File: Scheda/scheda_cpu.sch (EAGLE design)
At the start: 21 parts, among them IC3 LD1117V33

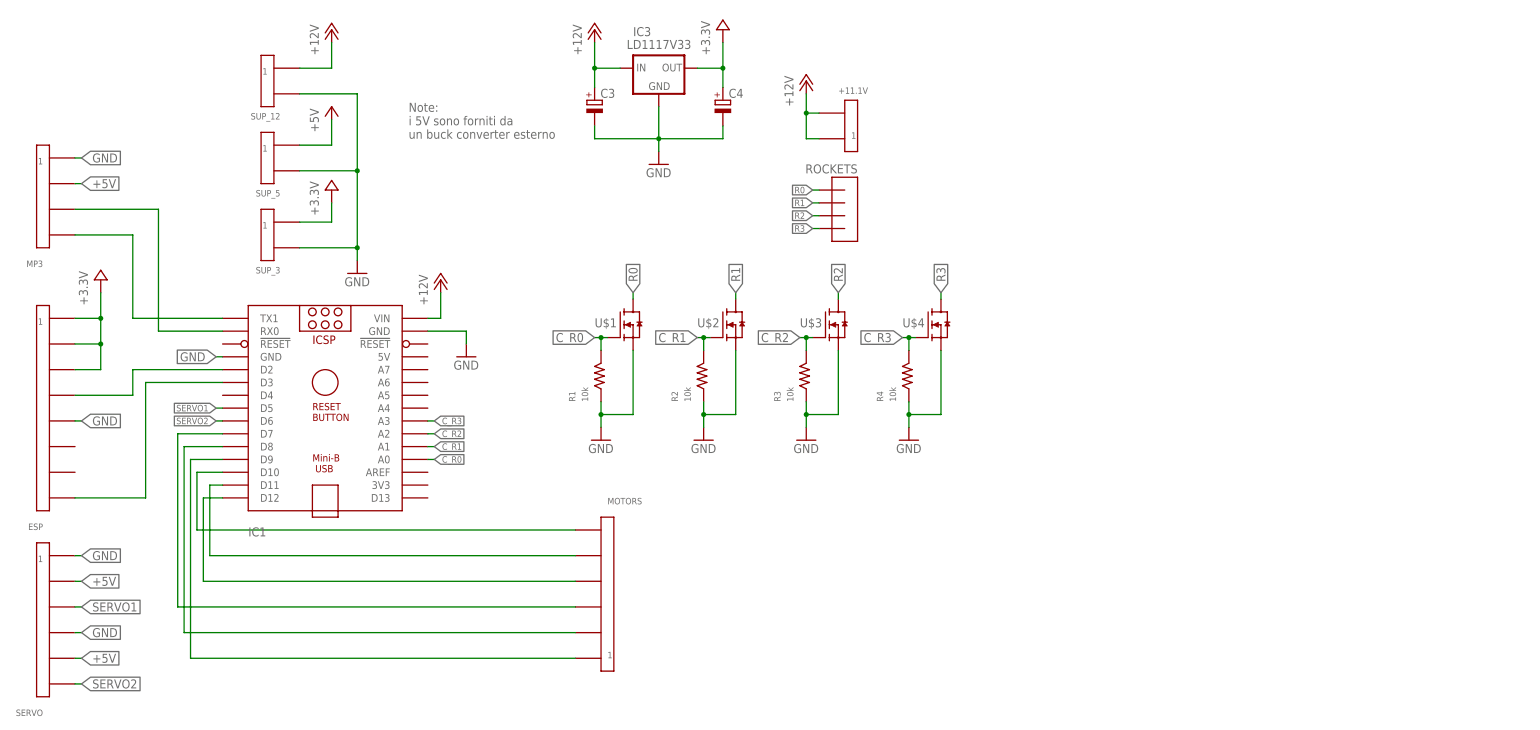
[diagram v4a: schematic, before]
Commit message: completato pcb con lm380
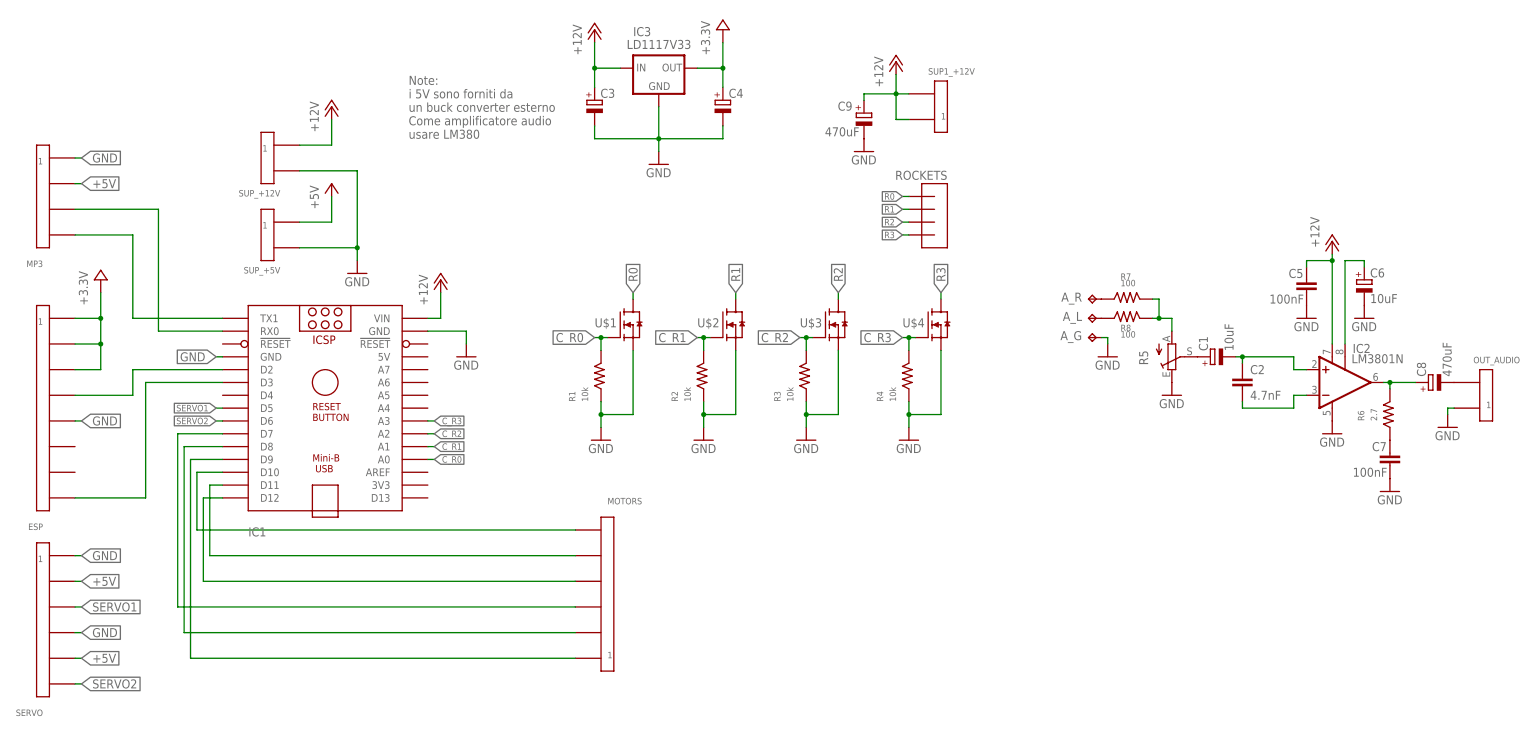
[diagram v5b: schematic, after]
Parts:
- removed +11.1V, SUP_12: AK500, roombarmato_eagle_lib:AK500
- added A_G, A_L, A_R: TPTP15SQ, testpad:TPTP15SQ
- added C1, C6: 10uF, roombarmato_eagle_lib:CPOL-EUE2.5-5
- added C2: 4.7nF, ITIS:C-EU025-030X050
- added C5, C7: 100nF, ITIS:C-EU025-030X050
- added C8, C9: 470uF, roombarmato_eagle_lib:CPOL-EUE2.5-5
- added IC2: LM3801N, roombarmato_eagle_lib:LM3801N
- added OUT_AUDIO, SUP1_+12V: AK500, roombarmato_eagle_lib:AK500
- added R5: (no value), pot:TRIM_EU-S64W
- added R6: 2.7, roombarmato_eagle_lib:RESISTOR1206
- added R7, R8: 100, roombarmato_eagle_lib:RESISTOR1206
- renumbered SUP_3 to SUP_+5V, SUP_5 to SUP_+12V
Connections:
- new net IN_AUDIO: R5.A, R7.P$2, R8.P$2
- new net N$10: C8.+, IC2.OUT, R6.P$2
- new net N$17: C8.-, OUT_AUDIO.P$2
- new net N$18: A_R.TP, R7.P$1
- new net N$19: A_L.TP, R8.P$1
- new net N$5: C1.+, R5.S
- new net N$6: C1.-, C2.1, IC2.+IN
- new net N$7: C2.2, IC2.-IN
- new net N$8: C6.+, IC2.BYPASS
- new net N$9: C7.1, R6.P$1
- net +12V: now also C5.1, C9.+, IC2.VSS, SUP1_+12V.P$1, SUP1_+12V.P$2, SUP_+12V.P$1; no longer +11.1V.P$1, +11.1V.P$2, SUP_12.P$1
- net +3.3V: no longer SUP_+5V.P$1
- net +5V: now also SUP_+5V.P$1; no longer SUP_+12V.P$1
- net GND: now also A_G.TP, C5.2, C6.-, C7.2, C9.-, IC2.GND, OUT_AUDIO.P$1, R5.E; no longer SUP_12.P$2
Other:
- note added: "Note: i 5V sono forniti da un buck converter esterno Come amplificatore audio usare LM380"
- note removed: "Note: i 5V sono forniti da un buck converter esterno"
- moved on the sheet: ROCKETS

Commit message: creato file excel ordine
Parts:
- C1, C6: device roombarmato_eagle_lib:CPOL-EUE2.5-5 -> ITIS:CPOL-EUE2-4
- C8: device roombarmato_eagle_lib:CPOL-EUE2.5-5 -> ITIS:CPOL-EUE3.5-8
- C9: value 470uF -> 1000uF; device roombarmato_eagle_lib:CPOL-EUE2.5-5 -> ITIS:CPOL-EUE3.5-10
- R5: value (none) -> 10k
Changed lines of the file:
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@@
 <part name="P+6" library="roombarmato_eagle_lib" deviceset="+12V" device=""/>
 <part name="IC2" library="roombarmato_eagle_lib" deviceset="LM380" device="N" package3d_urn="urn:adsk.eagle:package:16409/2" technology="1"/>
-<part name="R5" library="pot" library_urn="urn:adsk.eagle:library:331" deviceset="TRIM_EU-" device="S64W" package3d_urn="urn:adsk.eagle:package:22708/1"/>
+<part name="R5" library="pot" library_urn="urn:adsk.eagle:library:331" deviceset="TRIM_EU-" device="S64W" package3d_urn="urn:adsk.eagle:package:22708/1" value="10k"/>
 <part name="GND7" library="roombarmato_eagle_lib" deviceset="GND" device=""/>
-<part name="C1" library="roombarmato_eagle_lib" deviceset="CPOL-EU" device="E2.5-5" value="10uF"/>
+<part name="C1" library="ITIS" deviceset="CPOL-EU" device="E2-4" value="10uF"/>
 <part name="C2" library="ITIS" deviceset="C-EU" device="025-030X050" value="4.7nF"/>
 <part name="GND9" library="roombarmato_eagle_lib" deviceset="GND" device=""/>
 <part name="P+3" library="roombarmato_eagle_lib" deviceset="+12V" device=""/>
 <part name="GND10" library="roombarmato_eagle_lib" deviceset="GND" device=""/>
-<part name="C6" library="roombarmato_eagle_lib" deviceset="CPOL-EU" device="E2.5-5" value="10uF"/>
+<part name="C6" library="ITIS" deviceset="CPOL-EU" device="E2-4" value="10uF"/>
 <part name="GND11" library="roombarmato_eagle_lib" deviceset="GND" device=""/>
 <part name="R6" library="roombarmato_eagle_lib" deviceset="RESISTOR" device="1206" package3d_urn="urn:adsk.eagle:package:17825322/7" value="2.7"/>
@@
 <part name="C7" library="ITIS" deviceset="C-EU" device="025-030X050" value="100nF"/>
 <part name="GND12" library="roombarmato_eagle_lib" deviceset="GND" device=""/>
-<part name="C8" library="roombarmato_eagle_lib" deviceset="CPOL-EU" device="E2.5-5" value="470uF"/>
+<part name="C8" library="ITIS" deviceset="CPOL-EU" device="E3.5-8" value="470uF"/>
 <part name="OUT_AUDIO" library="roombarmato_eagle_lib" deviceset="AK500" device="" package3d_urn="urn:adsk.eagle:package:17855270/2"/>
 <part name="GND13" library="roombarmato_eagle_lib" deviceset="GND" device=""/>
@@
 <part name="A_G" library="testpad" library_urn="urn:adsk.eagle:library:385" deviceset="TP" device="TP15SQ" package3d_urn="urn:adsk.eagle:package:27975/1" value="TPTP15SQ"/>
 <part name="GND14" library="roombarmato_eagle_lib" deviceset="GND" device=""/>
-<part name="C9" library="roombarmato_eagle_lib" deviceset="CPOL-EU" device="E2.5-5" value="470uF"/>
+<part name="C9" library="ITIS" deviceset="CPOL-EU" device="E3.5-10" value="1000uF"/>
 <part name="GND15" library="roombarmato_eagle_lib" deviceset="GND" device=""/>
 </parts>
@@
 </instance>
 <instance part="R5" gate="1" x="167.64" y="5.08" smashed="yes" rot="MR180">
-<attribute name="NAME" x="162.941" y="6.35" size="1.778" layer="95" rot="MR270"/>
-<attribute name="VALUE" x="163.83" y="8.89" size="1.778" layer="96" rot="MR270"/>
+<attribute name="NAME" x="161.671" y="6.35" size="1.778" layer="95" rot="MR270"/>
+<attribute name="VALUE" x="163.83" y="6.35" size="1.778" layer="96" rot="MR270"/>
 </instance>
 <instance part="GND7" gate="1" x="167.64" y="-2.54" smashed="yes">
@@
 <instance part="C9" gate="G$1" x="106.68" y="53.34" smashed="yes">
 <attribute name="NAME" x="101.473" y="53.8226" size="1.778" layer="95"/>
-<attribute name="VALUE" x="98.933" y="48.7426" size="1.778" layer="96"/>
+<attribute name="VALUE" x="97.663" y="48.7426" size="1.778" layer="96"/>
 </instance>
 <instance part="GND15" gate="1" x="106.68" y="45.72" smashed="yes">

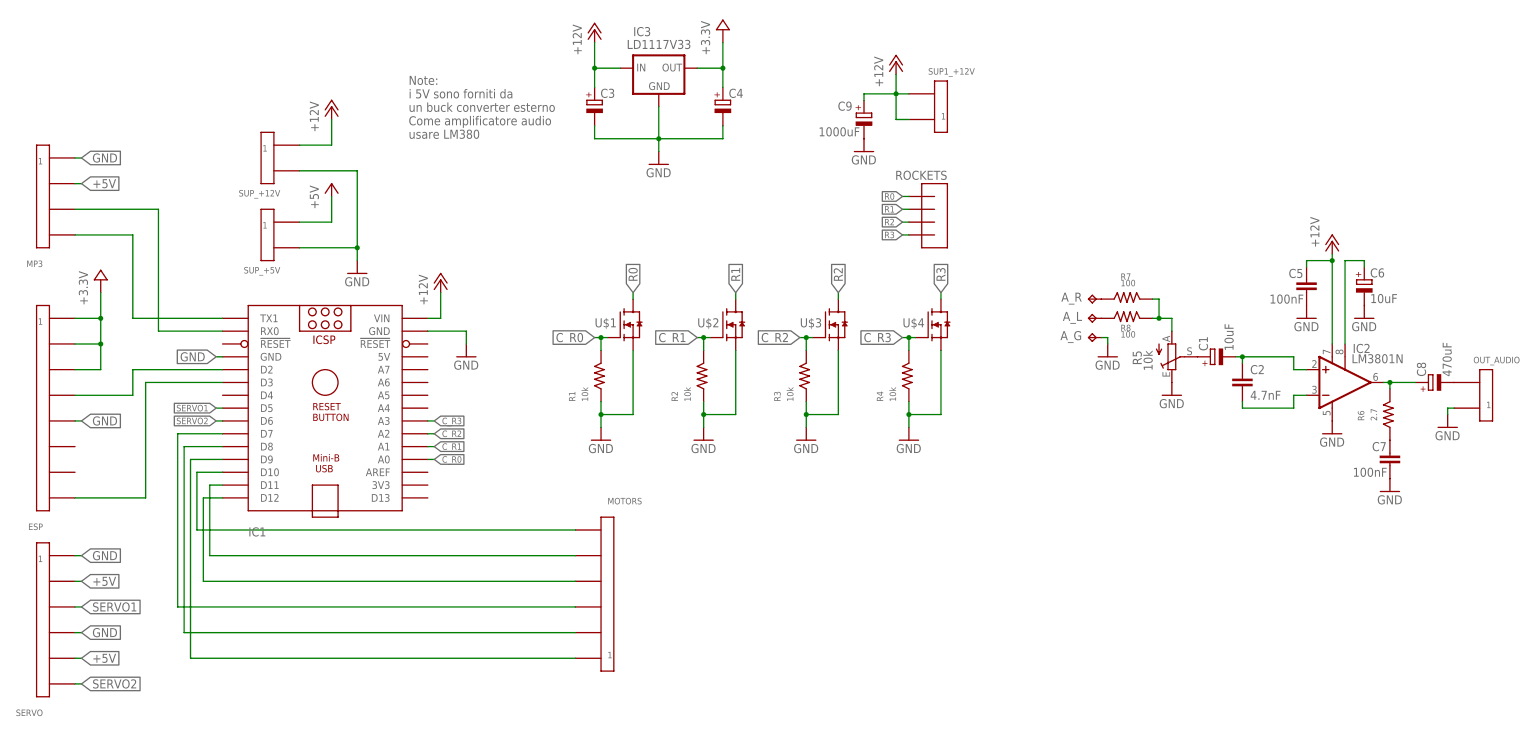
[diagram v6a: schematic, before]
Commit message: aggiunte etichette su pcb
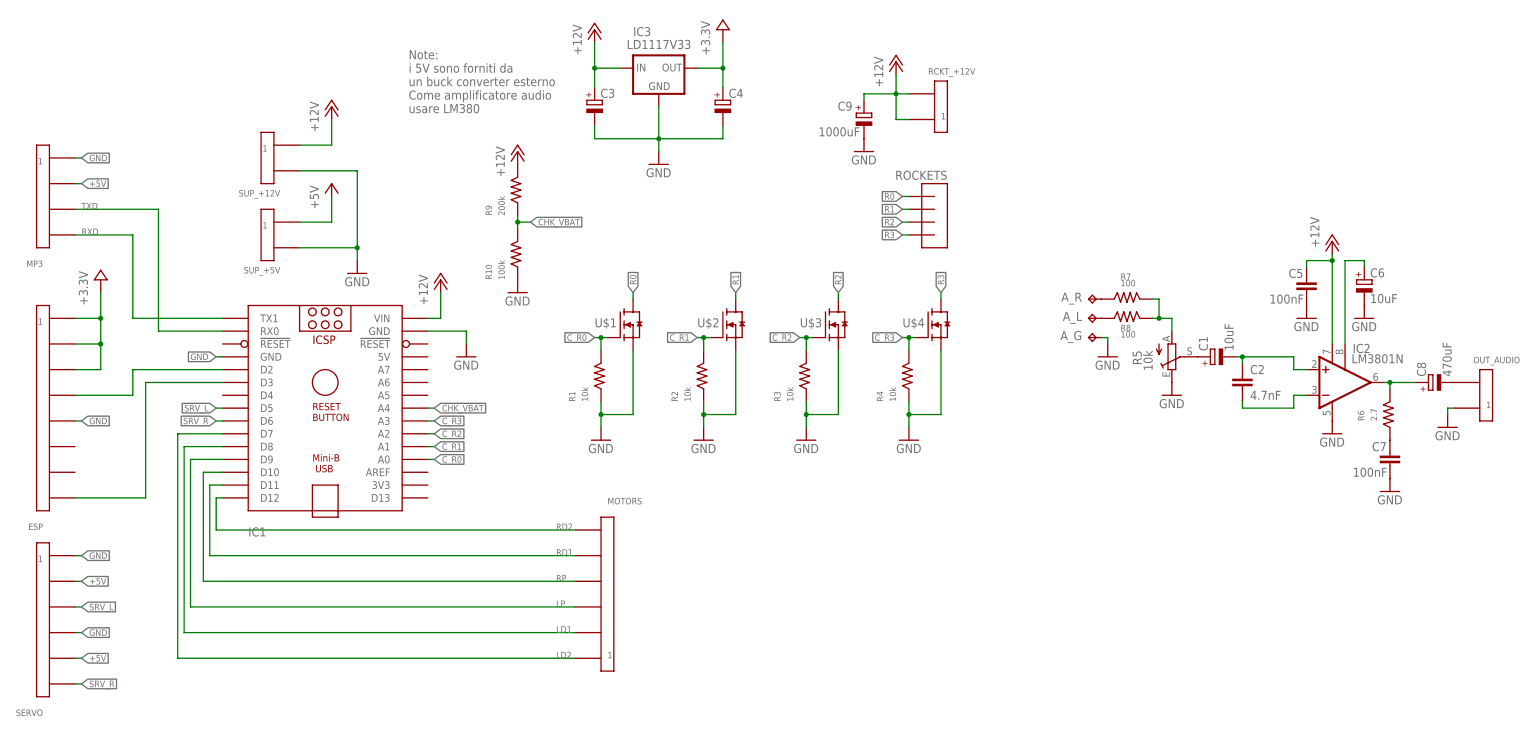
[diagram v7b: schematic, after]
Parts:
- added R10: 100k, roombarmato_eagle_lib:RESISTOR1206
- added R9: 200k, roombarmato_eagle_lib:RESISTOR1206
- renumbered SUP1_+12V to RCKT_+12V
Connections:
- net N$13 renamed LD1
- net N$16 renamed RD1
- net N$2 renamed TXD
- net N$3 renamed RXD
- net SERVO1 renamed SRV_L
- net SERVO2 renamed SRV_R
- removed net N$11: IC1.D10, MOTORS.P$6
- removed net N$12: IC1.D9, MOTORS.P$1
- removed net N$14: IC1.D7, MOTORS.P$3
- removed net N$15: IC1.D12, MOTORS.P$4
- new net CHK_VBAT: IC1.A4, R10.P$2, R9.P$1
- new net LD2: IC1.D7, MOTORS.P$1
- new net LP: IC1.D9, MOTORS.P$3
- new net RD2: IC1.D12, MOTORS.P$6
- new net RP: IC1.D10, MOTORS.P$4
- net +12V: now also R9.P$2
- net GND: now also R10.P$1

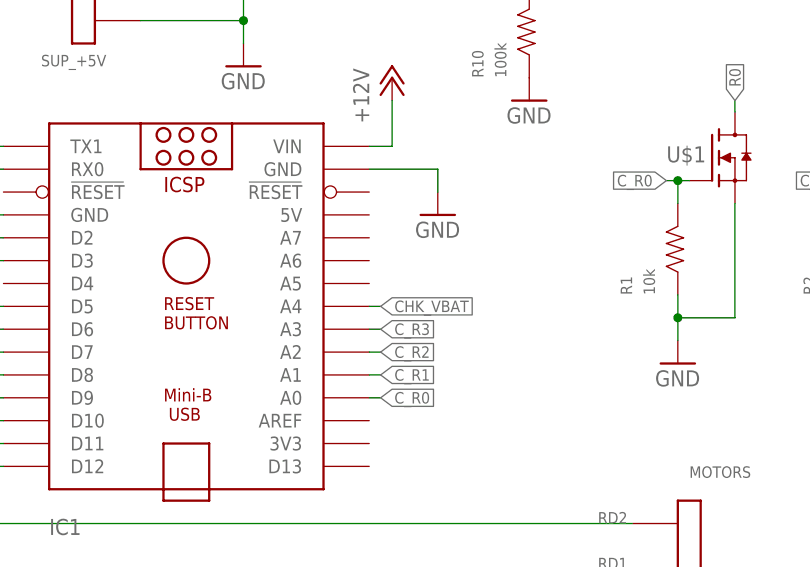
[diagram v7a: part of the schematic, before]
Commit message: create le cartelle test e ex
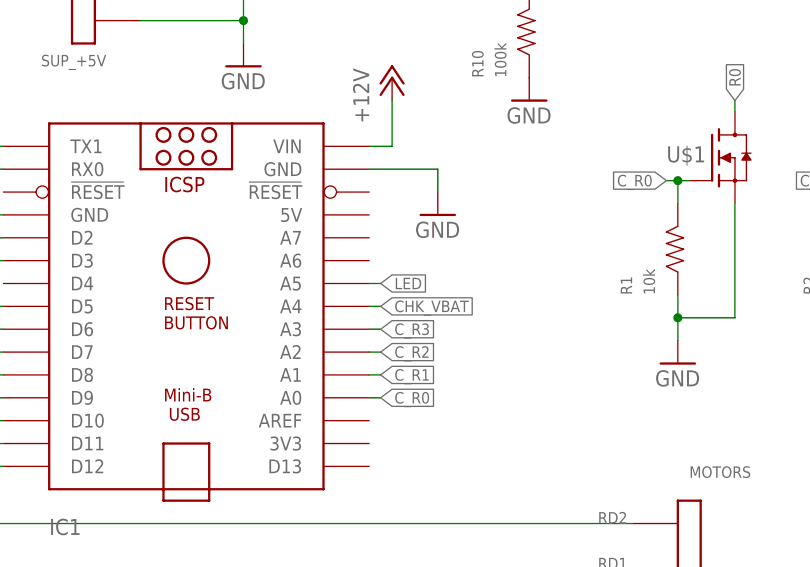
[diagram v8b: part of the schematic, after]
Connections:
- new net LED: IC1.A5
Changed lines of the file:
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@@
+</segment>
+</net>
+<net name="LED" class="0">
+<segment>
+<pinref part="IC1" gate="G$1" pin="A5"/>
+<wire x1="20.32" y1="-2.54" x2="21.59" y2="-2.54" width="0.1524" layer="91"/>
+<label x="21.59" y="-2.54" size="1.27" layer="95" xref="yes"/>
 </segment>
 </net>
